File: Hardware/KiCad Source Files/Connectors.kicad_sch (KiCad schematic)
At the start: 8 parts, among them J1 YK3210203000G, J2 USB4085-GF-A, J3 Conn_01x08, J4 YK3210203000G, J5 USB4085-GF-A, J6 USB1125-GF-B

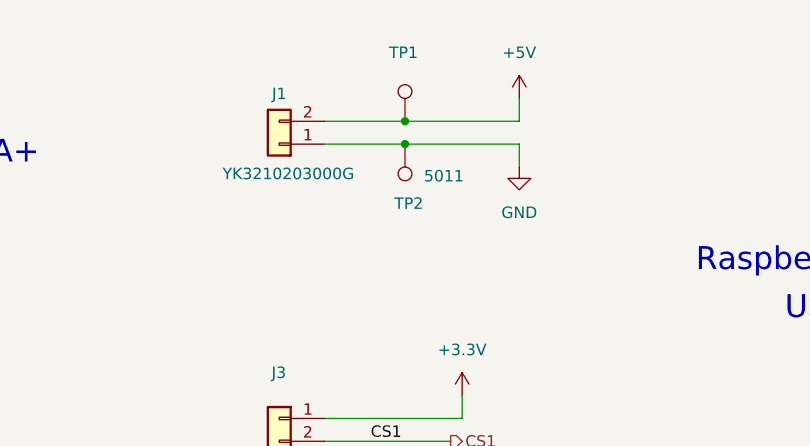
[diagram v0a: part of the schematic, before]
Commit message: Remove R6 from BOM and Centroid files.
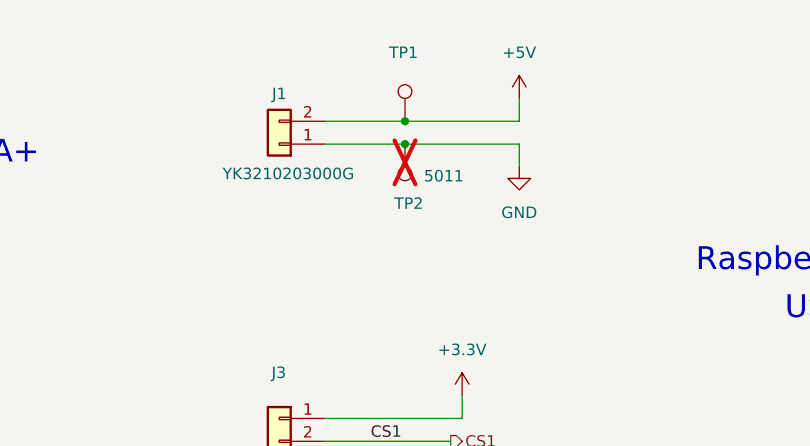
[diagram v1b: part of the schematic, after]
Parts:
- TP2: now not fitted
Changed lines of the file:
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@@
 		(in_bom yes)
 		(on_board yes)
-		(dnp no)
+		(dnp yes)
 		(property "Reference" "TP2"
 			(at 127.762 47.244 0)

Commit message: Finalized V3 Connector BOM based on testing on hardware.
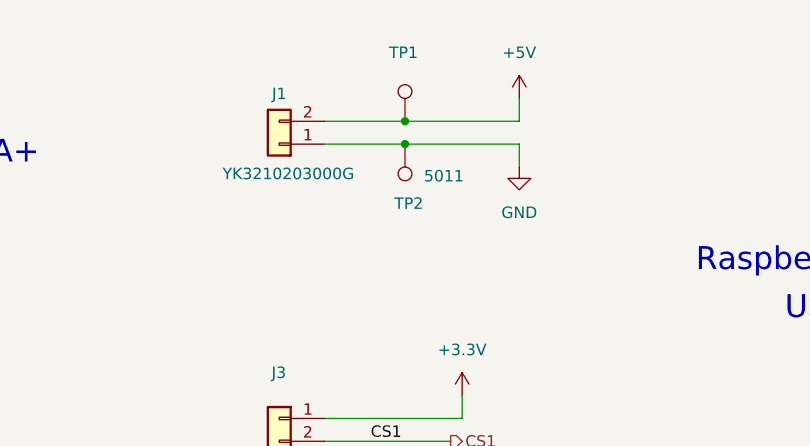
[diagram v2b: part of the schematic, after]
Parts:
- TP2: now fitted
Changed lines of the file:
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@@
 		(in_bom yes)
 		(on_board yes)
-		(dnp yes)
+		(dnp no)
 		(property "Reference" "TP2"
 			(at 127.762 47.244 0)
